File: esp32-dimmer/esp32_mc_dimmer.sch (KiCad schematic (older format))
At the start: 21 parts, among them J1 Conn_01x06, J2 Conn_01x04, J3 Conn_01x10, J4 Conn_01x02, J5 Conn_01x06, Q1 BUZ11, Q2 BUZ11, Q3 BUZ11, Q4 BUZ11, Q5 BUZ11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

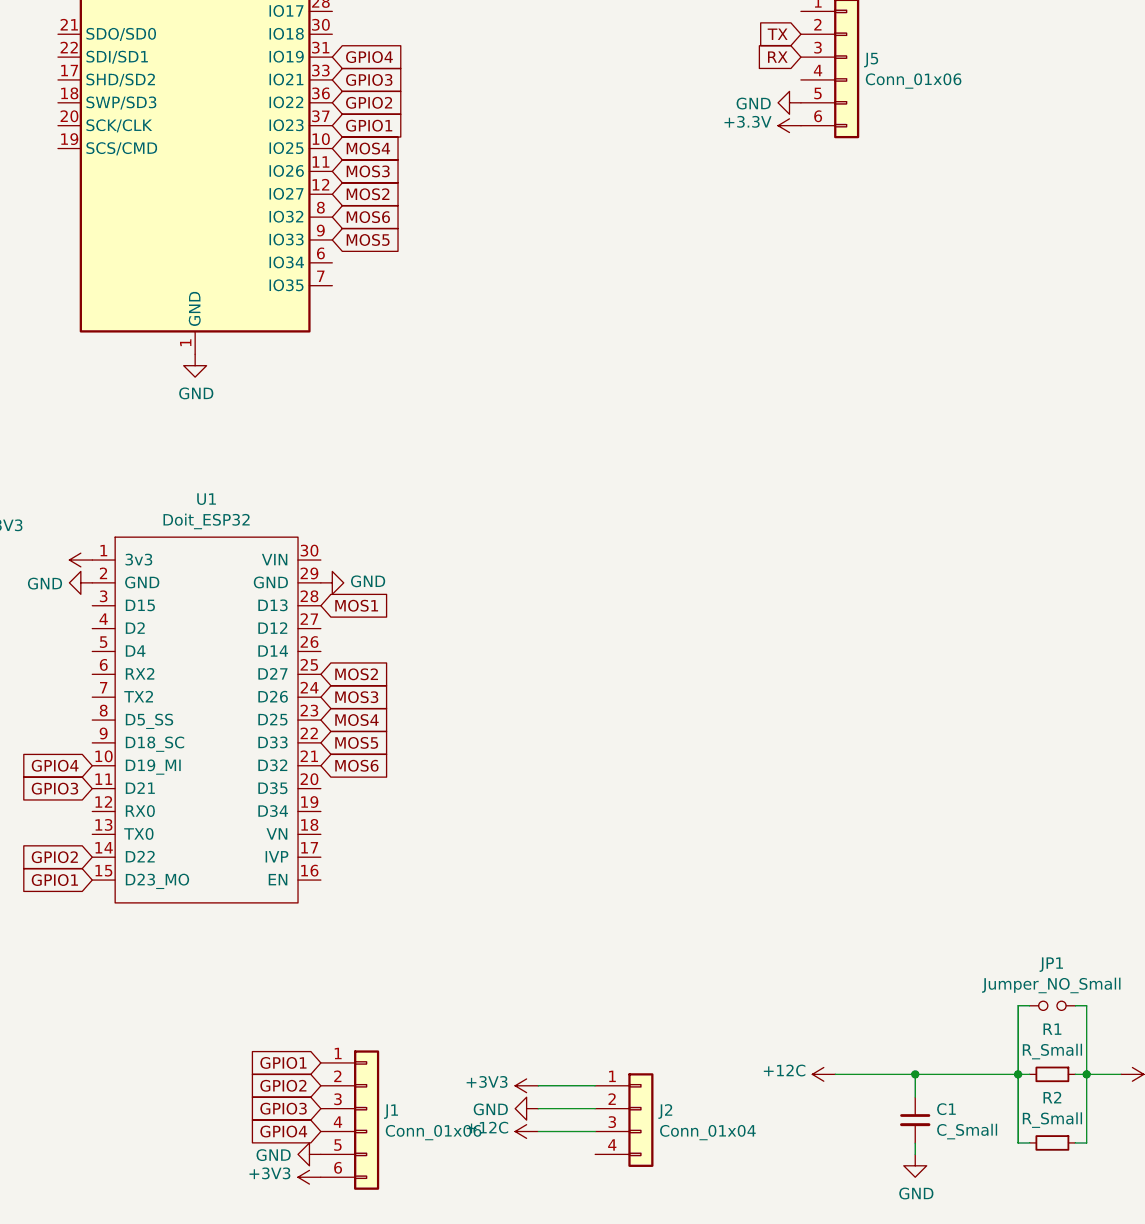
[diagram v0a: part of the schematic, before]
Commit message: Add new psu module and improve power layout
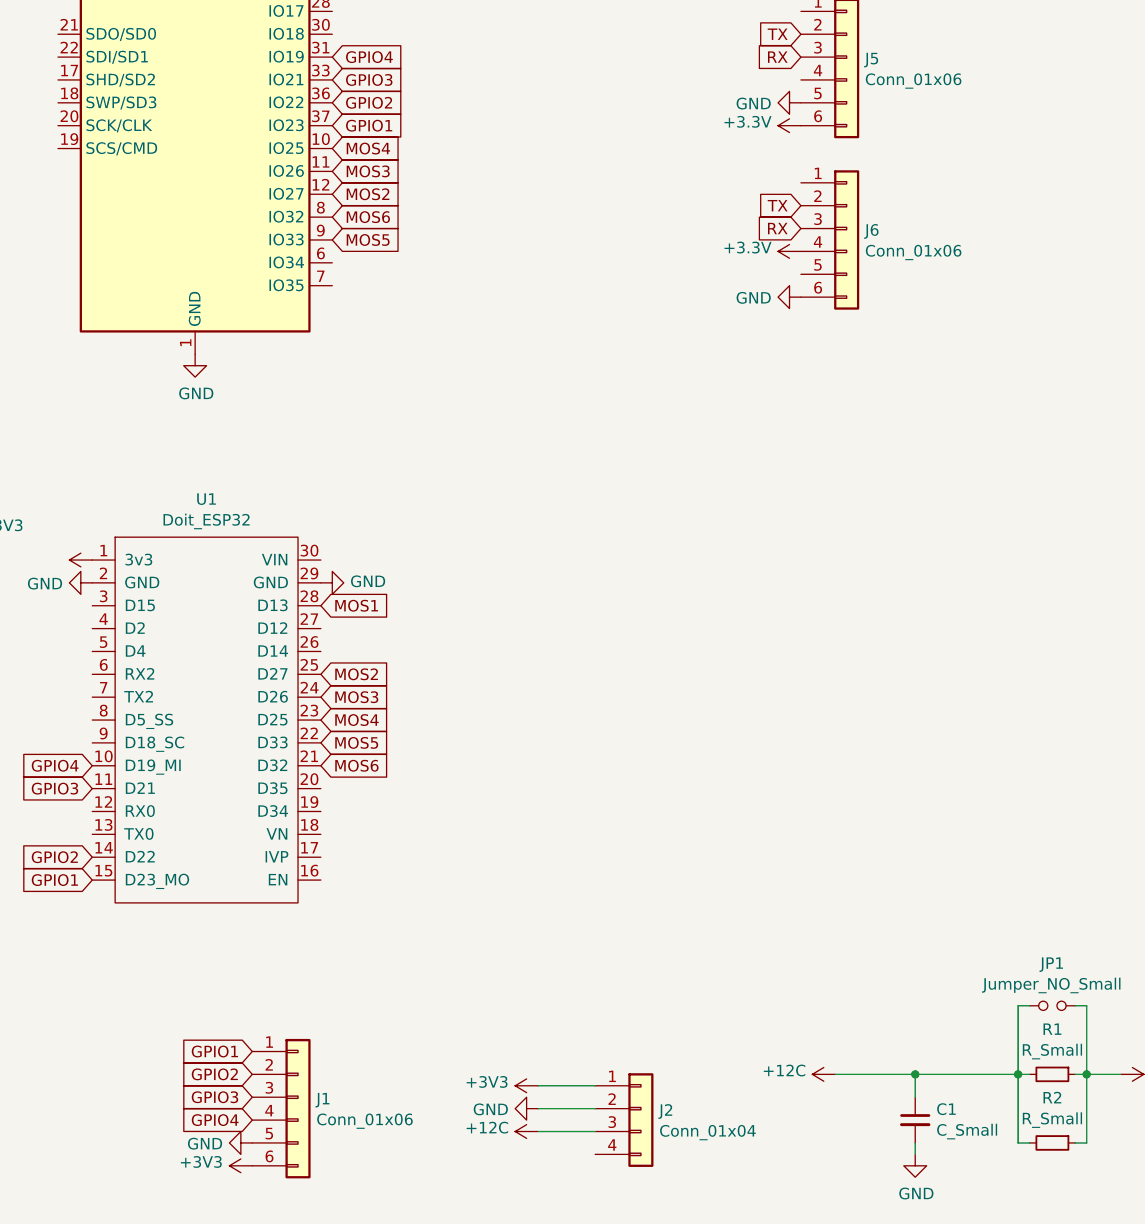
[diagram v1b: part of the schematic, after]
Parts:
- added J6: Conn_01x06, Connector_PinHeader_2.54mm:PinHeader_1x06_P2.54mm_Vertical, symbol Connector_Generic:Conn_01x06
- C1: footprint Capacitor_THT:CP_Radial_D7.5mm_P2.50mm -> Capacitor_THT:CP_Radial_D10.0mm_P2.50mm_P5.00mm
- J2: footprint aOmat_osat:4pin_reg_con -> Voltage-regulator:4pin_reg_con
- J3: footprint aOmat_osat:Phoenix_SPTAF_1_10-5,0-EL -> Phoenix-connect:Phoenix_SPTAF_1_10-5,0-EL
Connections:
- net +3V3: now also J6.4 (Pin_4)
- net GND: now also J6.6 (Pin_6)
- net RX: now also J6.3 (Pin_3)
- net TX: now also J6.2 (Pin_2)
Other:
- moved on the sheet: J1
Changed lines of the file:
@@
 F 0 "J3" H 10480 3392 50  0000 L CNN
 F 1 "Conn_01x10" H 10480 3301 50  0000 L CNN
-F 2 "aOmat_osat:Phoenix_SPTAF_1_10-5,0-EL" H 10400 3400 50  0001 C CNN
+F 2 "Phoenix-connect:Phoenix_SPTAF_1_10-5,0-EL" H 10400 3400 50  0001 C CNN
 F 3 "~" H 10400 3400 50  0001 C CNN
 	1    10400 3400
@@
 F 0 "J2" H 4480 7242 50  0000 L CNN
 F 1 "Conn_01x04" H 4480 7151 50  0000 L CNN
-F 2 "aOmat_osat:4pin_reg_con" H 4400 7250 50  0001 C CNN
+F 2 "Voltage-regulator:4pin_reg_con" H 4400 7250 50  0001 C CNN
 F 3 "~" H 4400 7250 50  0001 C CNN
 	1    4400 7250
@@
 F 0 "C1" H 5692 7346 50  0000 L CNN
 F 1 "C_Small" H 5692 7255 50  0000 L CNN
-F 2 "Capacitor_THT:CP_Radial_D7.5mm_P2.50mm" H 5600 7300 50  0001 C CNN
+F 2 "Capacitor_THT:CP_Radial_D10.0mm_P2.50mm_P5.00mm" H 5600 7300 50  0001 C CNN
 F 3 "~" H 5600 7300 50  0001 C CNN
 	1    5600 7300
@@
 L power:GND #PWR0121
 U 1 1 5D4BC88C
-P 3000 7450
-F 0 "#PWR0121" H 3000 7200 50  0001 C CNN
-F 1 "GND" V 3005 7322 50  0000 R CNN
-F 2 "" H 3000 7450 50  0001 C CNN
-F 3 "" H 3000 7450 50  0001 C CNN
-	1    3000 7450
+P 2700 7400
+F 0 "#PWR0121" H 2700 7150 50  0001 C CNN
+F 1 "GND" V 2705 7272 50  0000 R CNN
+F 2 "" H 2700 7400 50  0001 C CNN
+F 3 "" H 2700 7400 50  0001 C CNN
+	1    2700 7400
 	0    1    1    0
 $EndComp
@@
 L power:+3V3 #PWR0122
 U 1 1 5D4BB6C4
-P 3000 7550
-F 0 "#PWR0122" H 3000 7400 50  0001 C CNN
-F 1 "+3V3" V 3015 7678 50  0000 L CNN
-F 2 "" H 3000 7550 50  0001 C CNN
-F 3 "" H 3000 7550 50  0001 C CNN
-	1    3000 7550
-	0    -1   -1   0
-$EndComp
-Text GLabel 3000 7350 0    50   Input ~ 0
+P 2700 7500
+F 0 "#PWR0122" H 2700 7350 50  0001 C CNN
+F 1 "+3V3" V 2715 7628 50  0000 L CNN
+F 2 "" H 2700 7500 50  0001 C CNN
+F 3 "" H 2700 7500 50  0001 C CNN
+	1    2700 7500
+	0    -1   -1   0
+$EndComp
+Text GLabel 2700 7300 0    50   Input ~ 0
 GPIO4
-Text GLabel 3000 7250 0    50   Input ~ 0
+Text GLabel 2700 7200 0    50   Input ~ 0
 GPIO3
-Text GLabel 3000 7150 0    50   Input ~ 0
+Text GLabel 2700 7100 0    50   Input ~ 0
 GPIO2
-Text GLabel 3000 7050 0    50   Input ~ 0
+Text GLabel 2700 7000 0    50   Input ~ 0
 GPIO1
 $Comp
 L Connector_Generic:Conn_01x06 J1
 U 1 1 5D4B9455
-P 3200 7250
-F 0 "J1" H 3280 7242 50  0000 L CNN
-F 1 "Conn_01x06" H 3280 7151 50  0000 L CNN
-F 2 "Connector_PinHeader_2.54mm:PinHeader_1x06_P2.54mm_Vertical" H 3200 7250 50  0001 C CNN
-F 3 "~" H 3200 7250 50  0001 C CNN
-	1    3200 7250
+P 2900 7200
+F 0 "J1" H 2980 7192 50  0000 L CNN
+F 1 "Conn_01x06" H 2980 7101 50  0000 L CNN
+F 2 "Connector_PinHeader_2.54mm:PinHeader_1x06_P2.54mm_Vertical" H 2900 7200 50  0001 C CNN
+F 3 "~" H 2900 7200 50  0001 C CNN
+	1    2900 7200
 	1    0    0    -1
 $EndComp
@@
 Text GLabel 3050 1650 2    50   Input ~ 0
 RX
+$Comp
+L Connector_Generic:Conn_01x06 J6
+U 1 1 5F81D418
+P 5300 3400
+F 0 "J6" H 5380 3392 50  0000 L CNN
+F 1 "Conn_01x06" H 5380 3301 50  0000 L CNN
+F 2 "Connector_PinHeader_2.54mm:PinHeader_1x06_P2.54mm_Vertical" H 5300 3400 50  0001 C CNN
+F 3 "~" H 5300 3400 50  0001 C CNN
+	1    5300 3400
+	1    0    0    -1
+$EndComp
+Text GLabel 5100 3300 0    50   Input ~ 0
+TX
+Text GLabel 5100 3400 0    50   Input ~ 0
+RX
+$Comp
+L power:GND #PWR0131
+U 1 1 5F81D420
+P 5100 3700
+F 0 "#PWR0131" H 5100 3450 50  0001 C CNN
+F 1 "GND" V 5105 3572 50  0000 R CNN
+F 2 "" H 5100 3700 50  0001 C CNN
+F 3 "" H 5100 3700 50  0001 C CNN
+	1    5100 3700
+	0    1    1    0
+$EndComp
+$Comp
+L power:+3.3V #PWR0132
+U 1 1 5F81D426
+P 5100 3500
+F 0 "#PWR0132" H 5100 3350 50  0001 C CNN
+F 1 "+3.3V" V 5115 3628 50  0000 L CNN
+F 2 "" H 5100 3500 50  0001 C CNN
+F 3 "" H 5100 3500 50  0001 C CNN
+	1    5100 3500
+	0    -1   -1   0
+$EndComp
 $EndSCHEMATC

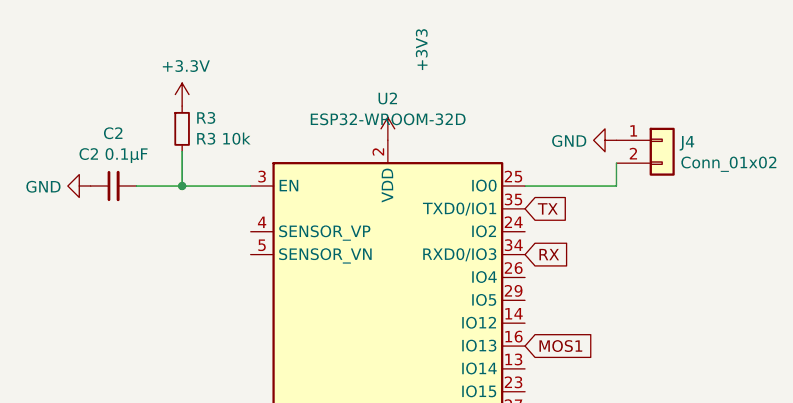
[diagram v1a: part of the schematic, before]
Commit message: Change resistor to lower inrush
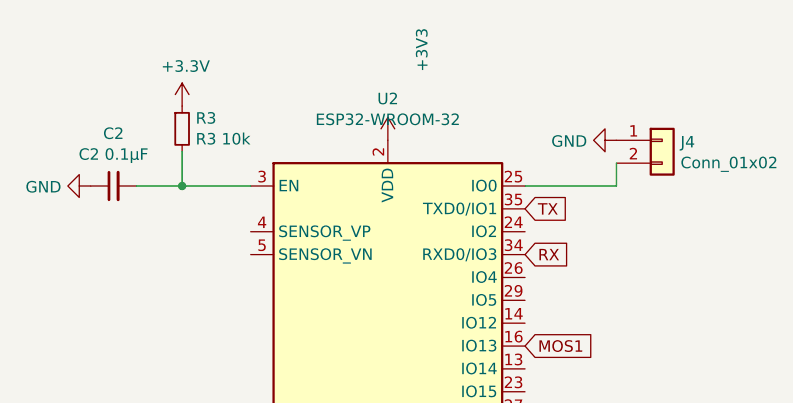
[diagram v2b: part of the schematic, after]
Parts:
- U2: value ESP32-WROOM-32D -> ESP32-WROOM-32
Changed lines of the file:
@@
 P 2450 2550
 F 0 "U2" H 2450 4131 50  0000 C CNN
-F 1 "ESP32-WROOM-32D" H 2450 4040 50  0000 C CNN
+F 1 "ESP32-WROOM-32" H 2450 4040 50  0000 C CNN
 F 2 "RF_Module:ESP32-WROOM-32" H 2450 1050 50  0001 C CNN
 F 3 "https://www.espressif.com/sites/default/files/documentation/esp32-wroom-32d_esp32-wroom-32u_datasheet_en.pdf" H 2150 2600 50  0001 C CNN
